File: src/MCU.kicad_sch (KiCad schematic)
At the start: 44 parts, among them J5 Conn_Coaxial, SW1 TS24CA, SW2 KH-6X6X7H-STM, U1 ESP32-C6, U17 WS2812, U18 WS2812, U20 WS2812, U3 W25Q64JVSSIQ, Y1 40MHz

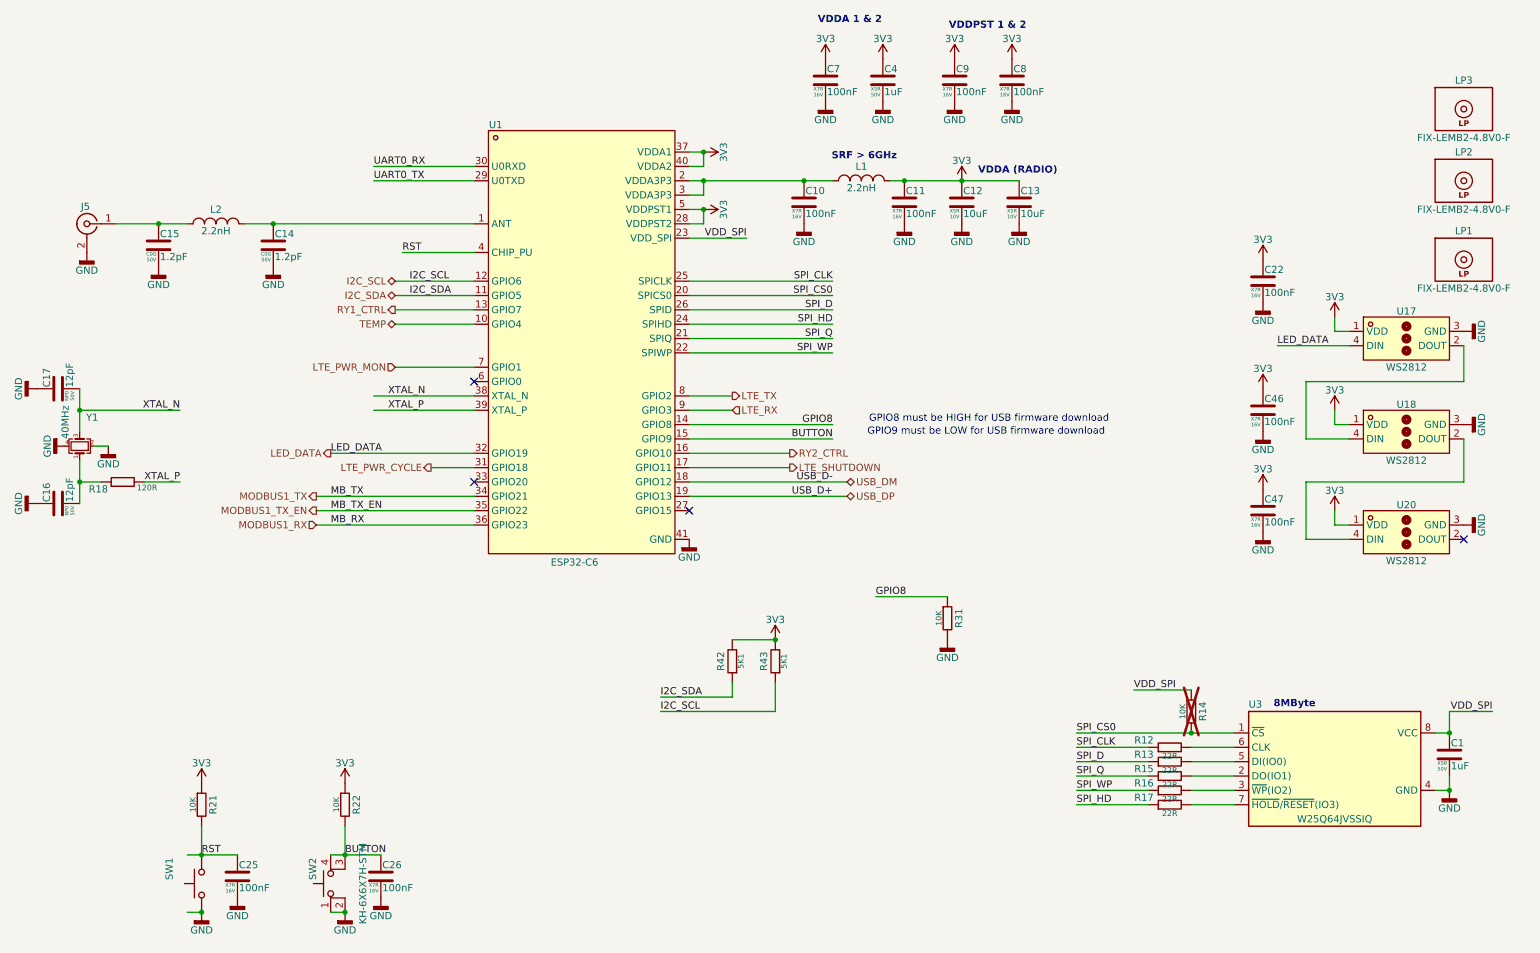
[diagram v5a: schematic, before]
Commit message: schematic cleanup, verification. GPIO9 pin pulldown changed to pullup.
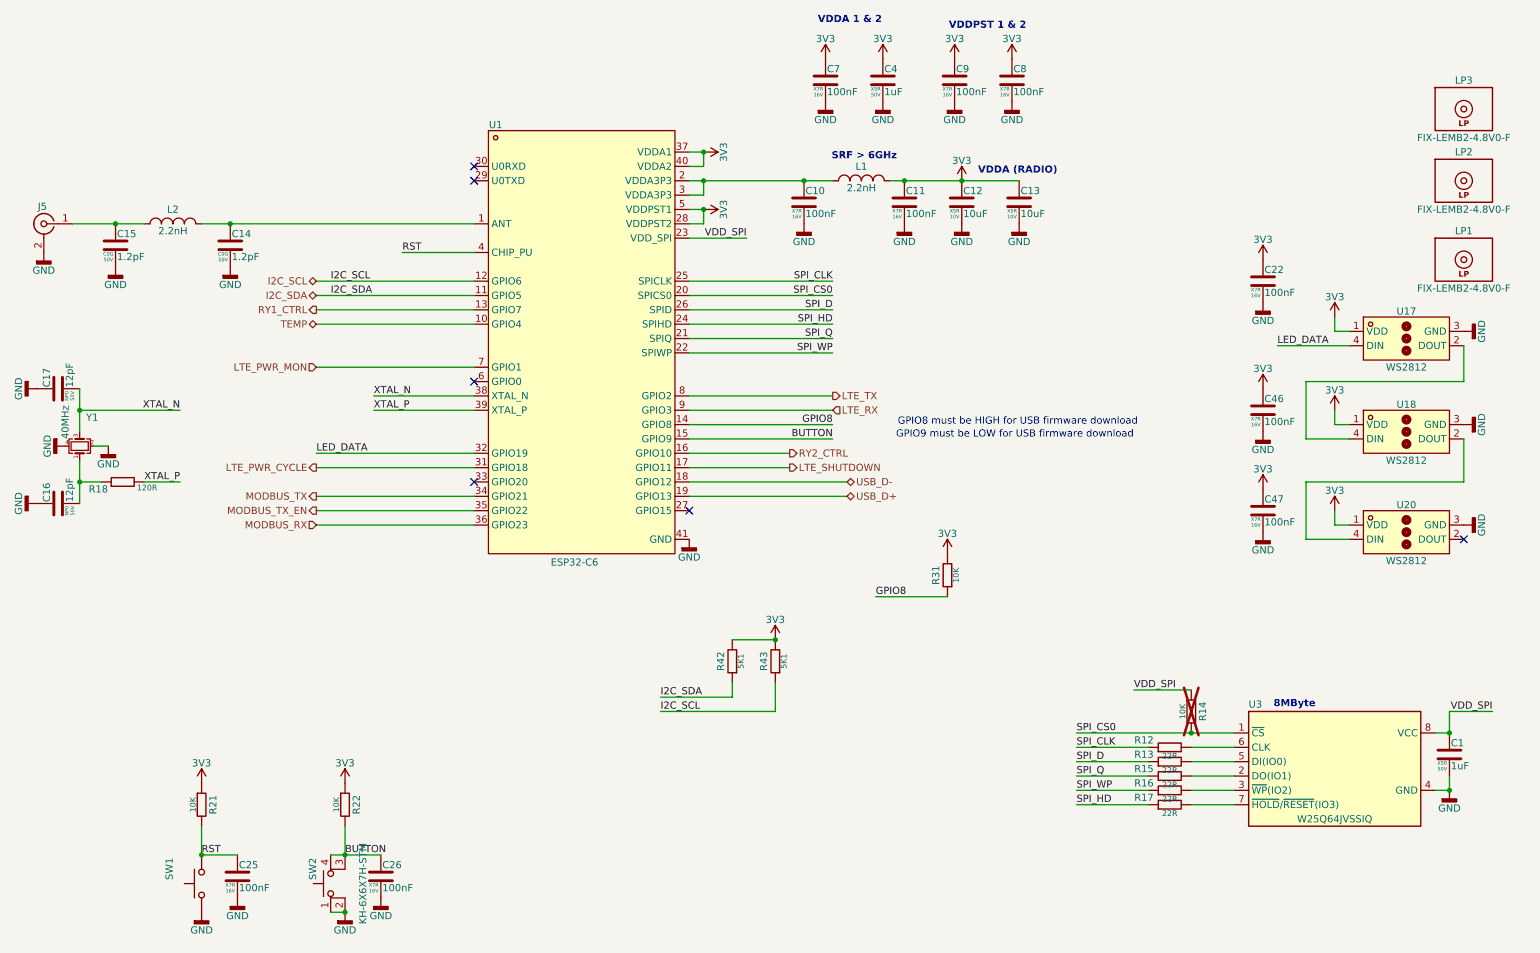
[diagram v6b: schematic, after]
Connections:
- net 3V3: now also R31.2
- net GND: no longer R31.2
- net MODBUS1_RX renamed MODBUS_RX
- net MODBUS1_TX renamed MODBUS_TX
- net MODBUS1_TX_EN renamed MODBUS_TX_EN
- net UART0_RX: no longer names the net of U1.30 (U0RXD)
- net UART0_TX: no longer names the net of U1.29 (U0TXD)
- net USB_DM renamed USB_D-
- net USB_DP renamed USB_D+
- no-connect marks 4 -> 6
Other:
- moved on the sheet: C14, C15, J5, L2, R31
